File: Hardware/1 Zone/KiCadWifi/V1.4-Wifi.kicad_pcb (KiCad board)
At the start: 2 copper layers, 100 x 80 mm, 133 parts, among them CN11 Pinheader 1x12 P2.54 Horizont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, CN16 Pinheader 1x02 P2.54 Horizont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, J1 Screw_Terminal_01x02, Q1 AOD4184A, Q10 PJA3404A, Q11 PJA3404A, Q12 BC816-16VL, Q8 UMH3NTN, SW1 K2-1102DP-G3SW-04, SW2 K2-1102DP-G3SW-04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

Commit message: Renamed TFT_LED, TFT_SI_OUT, TFT_SCK_OUT to LCD_* for consistency
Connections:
- net LCD_LED renamed TFT_LED
- net LCD_SCK_OUT renamed TFT_SCK_OUT
- net LCD_SI_OUT renamed TFT_SI_OUT

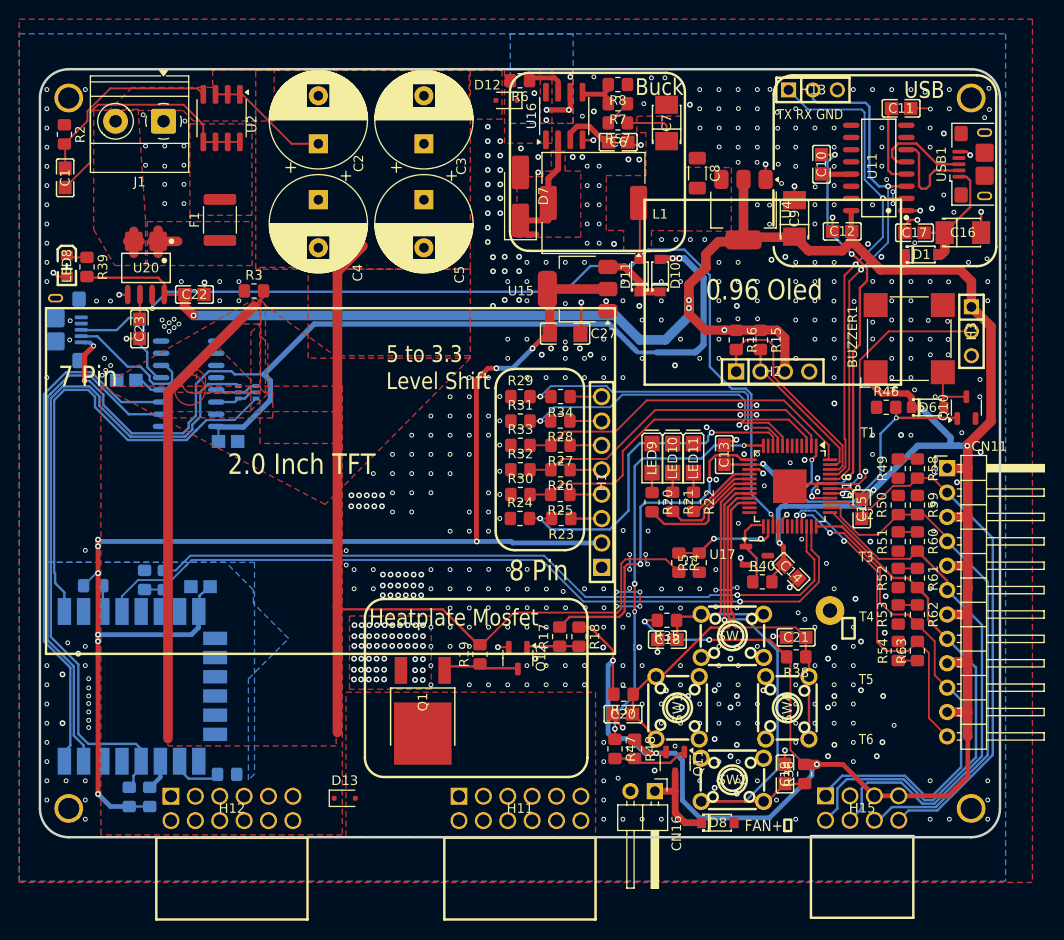
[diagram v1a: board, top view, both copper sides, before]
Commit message: E_TX, R_TX return paths tightened
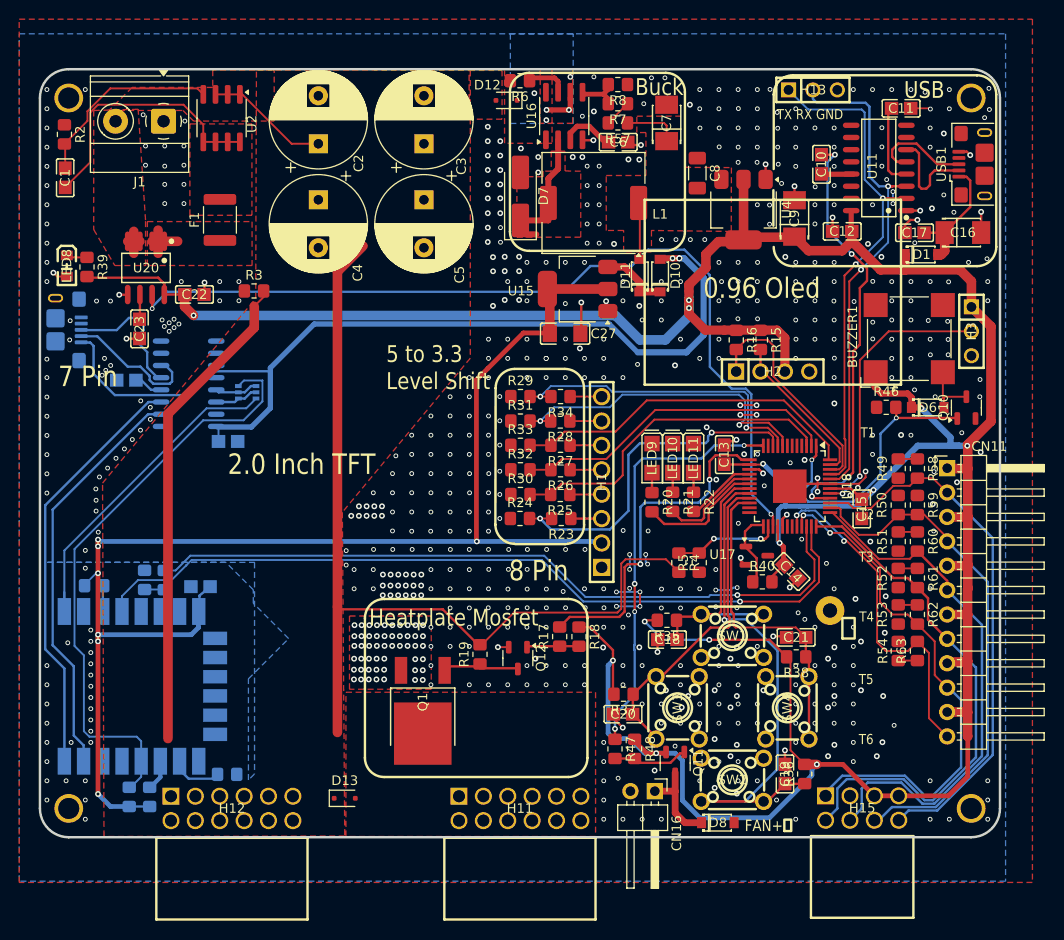
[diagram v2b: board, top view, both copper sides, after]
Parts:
- moved R43 0.10 mm to (105.7, 123.8)
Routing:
- net E_RESET: track 48.5 -> 34.9 mm
- net ESP_BOOT: track 74.5 -> 62.1 mm
- net E_RX: track 53.9 -> 43.0 mm
- net E_TX: track 54.1 -> 44.0 mm
- net VUSB_ESP: track 104.9 -> 96.7 mm, vias 5 -> 3
- net 3.3V: track 141.5 -> 141.4 mm, vias 9 -> 7
- net GND: vias 652 -> 698
- net +5V: vias 14 -> 13

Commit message: Cleaning. Simplified segmented traces.
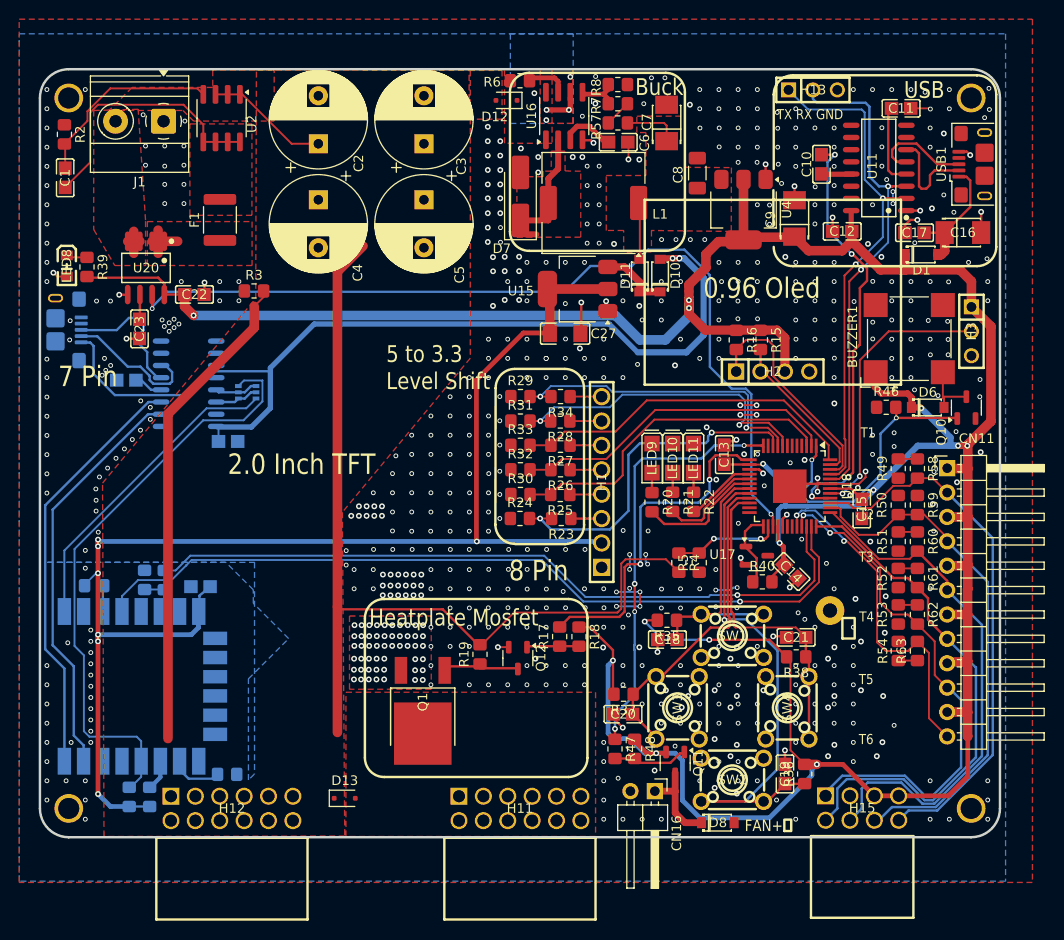
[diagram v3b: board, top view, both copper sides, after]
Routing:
- net +5V: track 361.8 -> 359.4 mm, vias 13 -> 14
- net E_RESET: track 34.9 -> 32.9 mm
- net THERMISTOR2: track 55.5 -> 53.9 mm
- net GND: track 68.9 -> 67.3 mm, vias 698 -> 696
- net Net-(D7-K): track 15.2 -> 13.6 mm
- net SWD_LEFT: track 33.9 -> 32.6 mm
- net IO15: track 5.15 -> 3.88 mm
- net MEGA_RX: track 85.7 -> 84.5 mm
- net RXD3.3: track 4.86 -> 3.91 mm
- net 3.3V: track 141.4 -> 140.5 mm
- net Net-(Q1-G): track 7.59 -> 6.75 mm
- net THERMISTOR5: track 54.1 -> 53.5 mm
- net Net-(Q11-G): track 7.82 -> 7.17 mm
- net SWD_UP: track 28.6 -> 27.9 mm
- net VUSB_ESP: track 96.7 -> 97.2 mm
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
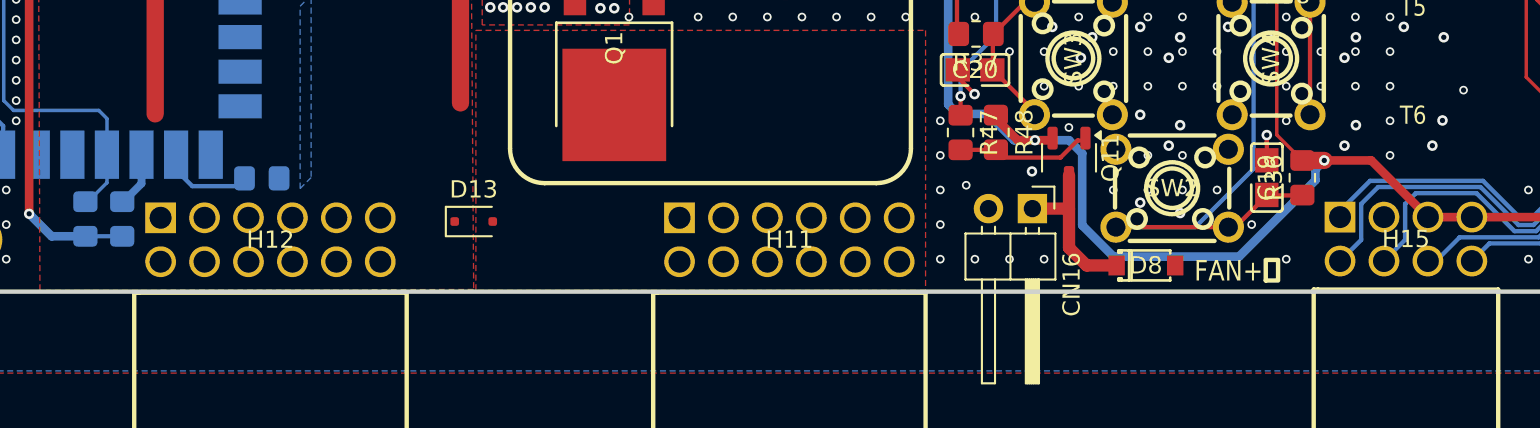
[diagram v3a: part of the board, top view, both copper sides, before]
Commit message: Moved D8 for EMC reasons. Refactored Fan ctrl schematic. BOM details corrected.
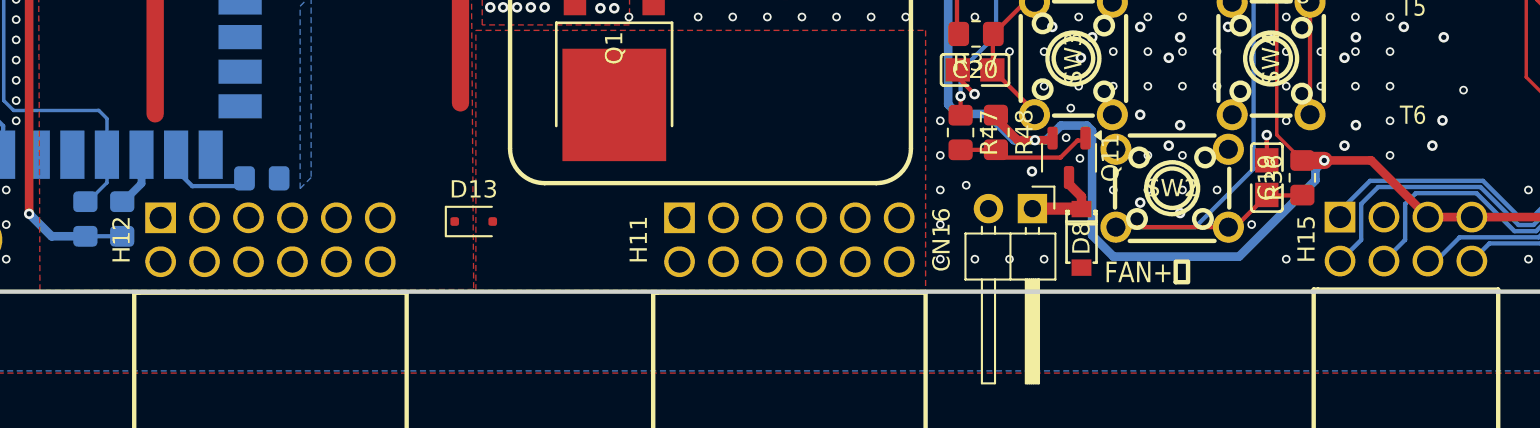
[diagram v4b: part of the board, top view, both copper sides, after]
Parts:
- H11, H12: value A2541HWR-2x6P -> 68021-412HLF
- H15: value A2541HWR-2x4P -> 68021-208HLF
- Q1: value AOD4184A -> IPD90N04S403ATMA1
- moved D8 4.04 mm to (166.9, 146.9), turned to -90 degrees
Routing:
- net /FANOUT: track 9.51 -> 4.98 mm
- net +5V: track 359.4 -> 361.2 mm
- net GND: vias 696 -> 698

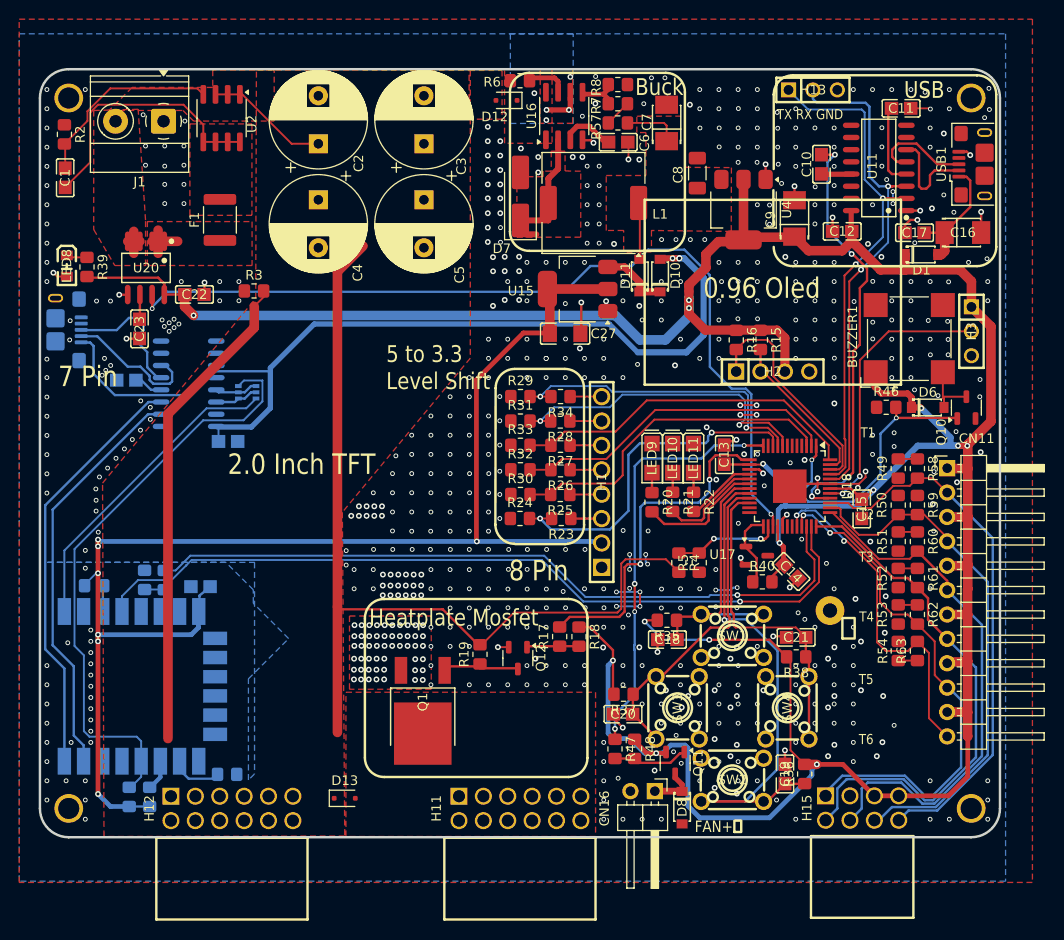
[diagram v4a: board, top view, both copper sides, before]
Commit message: BOM detailes corrected
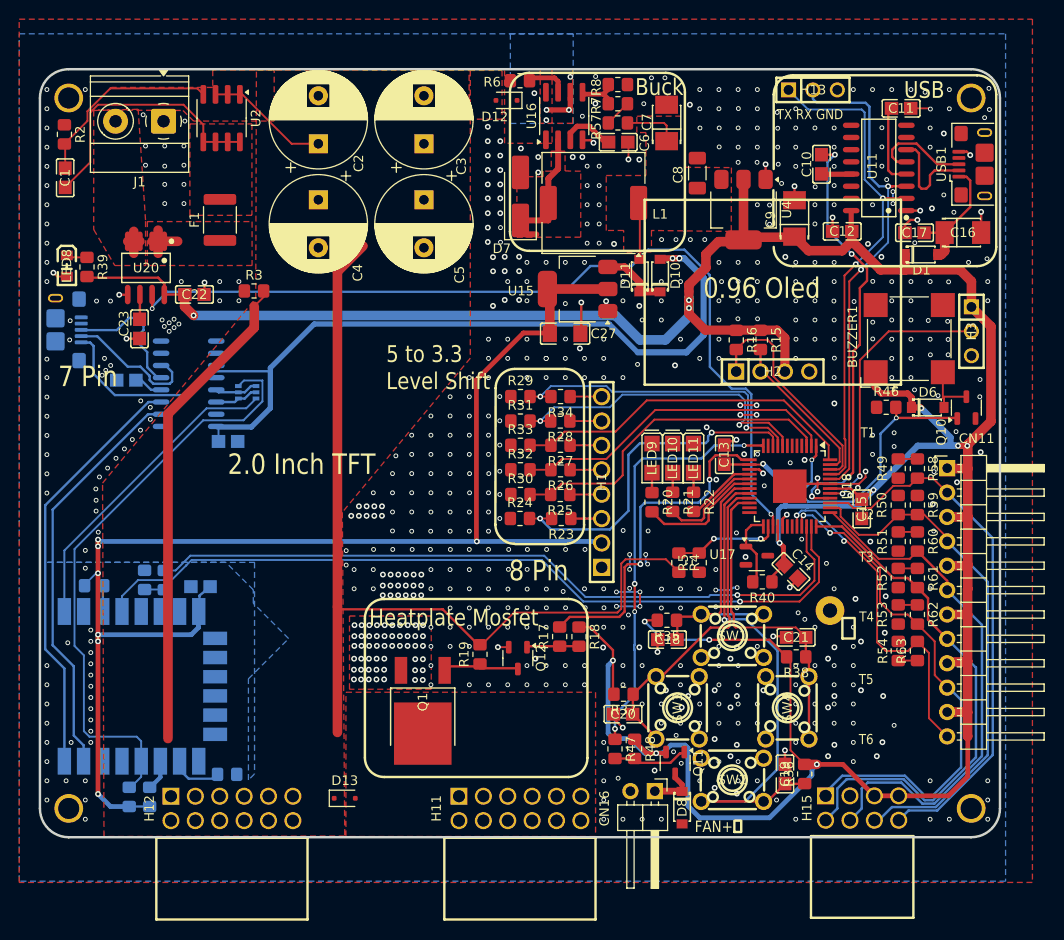
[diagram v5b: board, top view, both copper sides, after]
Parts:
- R39: value 750 0805 -> 750R 0805
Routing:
- net GND: track 67.3 -> 66.4 mm
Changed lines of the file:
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@@
 			)
 		)
-		(property "Datasheet" "https://atta.szlcsc.com/upload/public/pdf/source/20130706/1457706622210.pdf"
+		(property "Datasheet" "https://www.mouser.dk/datasheet/2/1115/ACS712_Datasheet-3178682.pdf"
 			(at 0 0 180)
 			(layer "F.Fab")
@@
 		(tags "resistor handsolder")
 		(property "Reference" "R40"
-			(at 0 -1.65 0)
+			(at 0 1.65 0)
 			(layer "F.SilkS")
 			(effects
@@
 			)
 		)
-		(property "Datasheet" ""
+		(property "Datasheet" "https://eu.mouser.com/datasheet/2/392/n_catalog_partition09_en-1620720.pdf"
 			(at 0 0 180)
 			(unlocked yes)
@@
 			)
 		)
+		(property "Manufacturer" "Susumu"
+			(at 0 0 180)
+			(unlocked yes)
+			(layer "F.Fab")
+			(hide yes)
+			(effects
+				(font
+					(size 1 1)
+					(thickness 0.15)
+				)
+			)
+		)
+		(property "mpn" "KRL1220E-M-R330-F"
+			(at 0 0 180)
+			(unlocked yes)
+			(layer "F.Fab")
+			(hide yes)
+			(effects
+				(font
+					(size 1 1)
+					(thickness 0.15)
+				)
+			)
+		)
 		(sheetname "/")
 		(sheetfile "V1.4-Wifi.kicad_sch")
@@
 		(tags "SOIC SO")
 		(property "Reference" "U2"
-			(at 0.599 -3.159 90)
+			(at 0 -3.577 90)
 			(layer "F.SilkS")
 			(effects
@@
 			)
 		)
-		(property "Value" "750 0805"
+		(property "Value" "750R 0805"
 			(at 0 1.65 90)
 			(layer "F.Fab")
@@
 		(at 178.232 122.324 -45)
 		(property "Reference" "C14"
-			(at 0 0 315)
+			(at -0.004243 -1.726755 315)
 			(layer "F.SilkS")
 			(effects
@@
 		(at 110.3735 97.049 -90)
 		(property "Reference" "C23"
-			(at 0 0 270)
+			(at -0.549 1.6235 270)
 			(layer "F.SilkS")
 			(effects
@@
 	)
 	(segment
-		(start 173 120.9)
-		(end 173 121.182)
-		(width 0.25)
-		(layer "F.Cu")
-		(net 1)
-	)
-	(segment
 		(start 192.6775 74.0775)
 		(end 190.7 74.0775)
@@
 	)
 	(segment
-		(start 173 121.182)
-		(end 173.441 121.623)
-		(width 0.25)
-		(layer "F.Cu")
-		(net 1)
-	)
-	(segment
 		(start 172.95 105)
 		(end 174.65 105)
@@
 	)
 	(via
-		(at 173 120.9)
+		(at 173.5 120.8)
 		(size 0.61)
 		(drill 0.305)
@@
 	)
 	(via
-		(at 172.75 117.3)
+		(at 172.55 118.3)
 		(size 0.5)
 		(drill 0.3)
@@
 	)
 	(segment
+		(start 175.355 117.484)
+		(end 174.121 117.484)
+		(width 0.25)
+		(layer "F.Cu")
+		(net 44)
+	)
+	(segment
+		(start 174.65 122.9115)
+		(end 174.65 120.5)
+		(width 0.25)
+		(layer "F.Cu")
+		(net 44)
+	)
+	(segment
 		(start 174.121 117.484)
-		(end 173.441 118.164)
+		(end 173.55 118.055)
 		(width 0.25)
 		(layer "F.Cu")
@@
 	)
 	(segment
-		(start 173.441 118.164)
-		(end 173.441 119.723)
+		(start 173.55 118.055)
+		(end 173.55 119.7115)
 		(width 0.25)
 		(layer "F.Cu")
@@
 	)
 	(segment
-		(start 174.65 120.932)
-		(end 174.65 122.9115)
+		(start 174.65 120.5)
+		(end 173.873 119.723)
 		(width 0.25)
 		(layer "F.Cu")
@@
 	)
 	(segment
-		(start 173.441 119.723)
-		(end 174.65 120.932)
+		(start 173.55 119.7115)
+		(end 173.5385 119.723)
 		(width 0.25)
 		(layer "F.Cu")
@@
 	)
 	(segment
-		(start 175.355 117.484)
-		(end 174.121 117.484)
+		(start 173.873 119.723)
+		(end 173.5385 119.723)
 		(width 0.25)
 		(layer "F.Cu")
@@
 		(polygon
 			(pts
-				(xy 118 70.1) (xy 118 71.9) (xy 109.6 71.9) (xy 107.2 74.3) (xy 114.9 74.3) (xy 116 75.4) (xy 124.4 75.4)
+				(xy 118 70.1) (xy 118 71.9) (xy 107.45 71.9) (xy 105.05 74.25) (xy 114.9 74.3) (xy 116 75.4) (xy 124.4 75.4)
 				(xy 124.4 70.1)
 			)
